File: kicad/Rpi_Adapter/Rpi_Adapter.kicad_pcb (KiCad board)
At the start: 2 copper layers, 42 x 68 mm, 8 parts, among them P1 CONN_02X20, P2 CONN_02X03

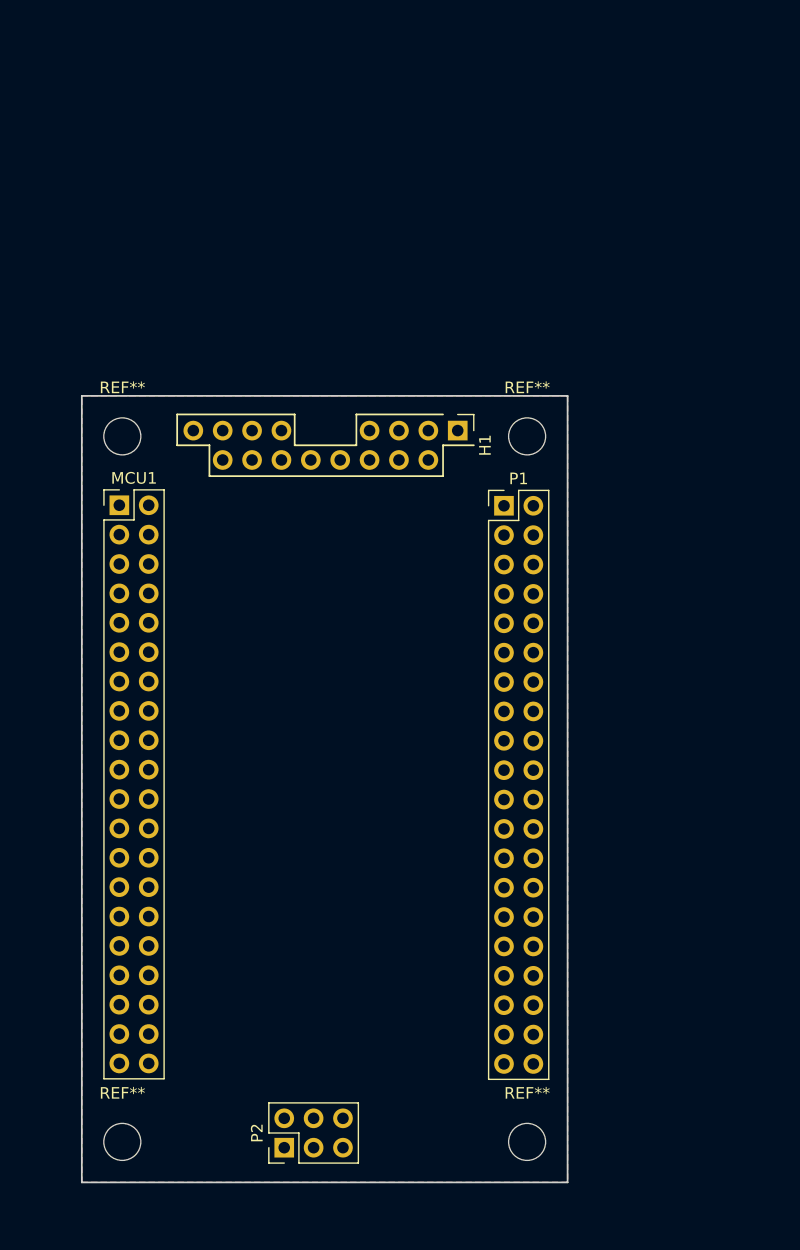
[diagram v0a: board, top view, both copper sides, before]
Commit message: Layout done and 2L_1 is sent to OSH Park
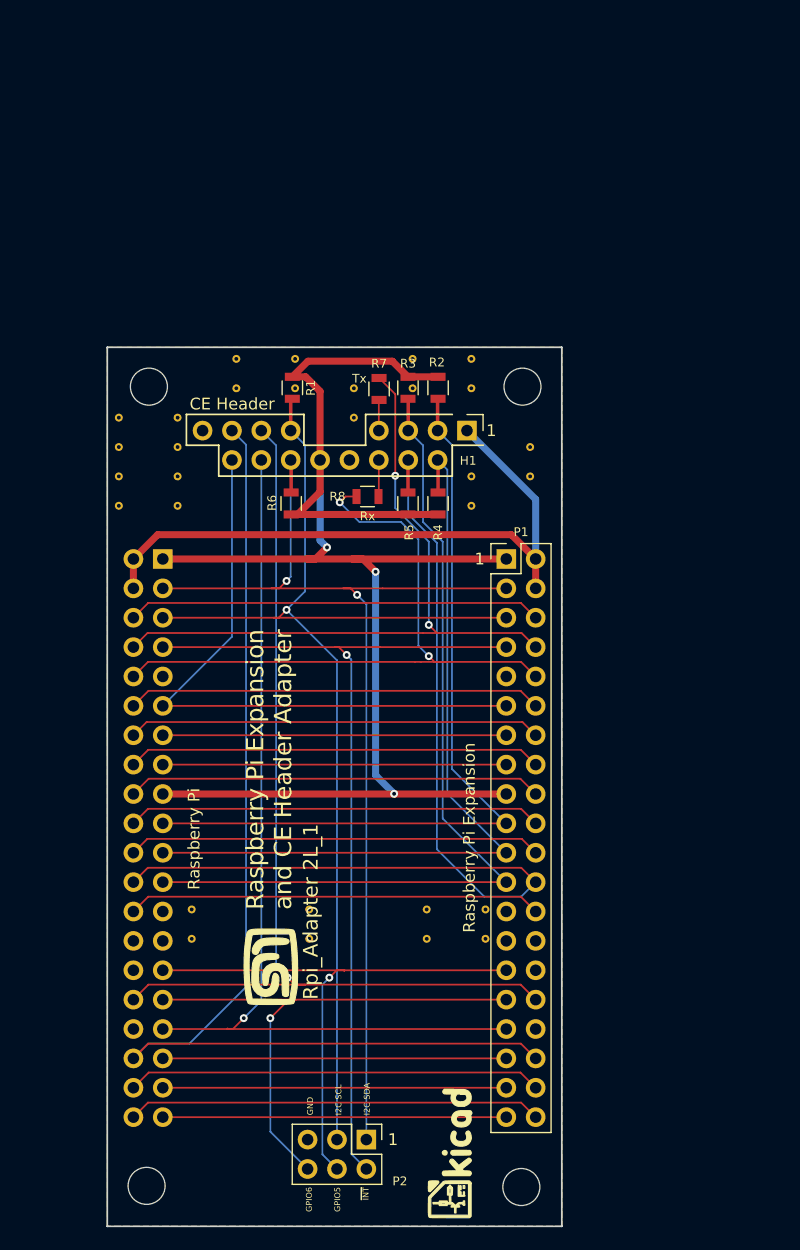
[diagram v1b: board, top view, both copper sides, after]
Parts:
- added 1: Stitch, Rpi_Adapter_Footprints:Stitch, F.Cu at (170.5, 97.4)
- added 11: Stitch, Rpi_Adapter_Footprints:Stitch, F.Cu at (190.8, 99.9)
- added 12: Stitch, Rpi_Adapter_Footprints:Stitch, F.Cu at (195.9, 99.9)
- added 3: Stitch, Rpi_Adapter_Footprints:Stitch, F.Cu at (180.7, 97.4)
- added 5: Stitch, Rpi_Adapter_Footprints:Stitch, F.Cu at (190.8, 97.4)
- added 6: Stitch, Rpi_Adapter_Footprints:Stitch, F.Cu at (195.9, 97.4)
- added 7: Stitch, Rpi_Adapter_Footprints:Stitch, F.Cu at (170.5, 99.9)
- added 9: Stitch, Rpi_Adapter_Footprints:Stitch, F.Cu at (180.7, 99.9)
- added ?: Stitch, Rpi_Adapter_Footprints:Stitch, F.Cu at (194.7, 62.5)
- added ?: Stitch, Rpi_Adapter_Footprints:Stitch, F.Cu at (164.2, 57.4)
- added ?: Stitch, Rpi_Adapter_Footprints:Stitch, F.Cu at (184.5, 54.9)
- added ?: Stitch, Rpi_Adapter_Footprints:Stitch, F.Cu at (169.3, 54.9)
- added ?: Stitch, Rpi_Adapter_Footprints:Stitch, F.Cu at (164.2, 54.9)
- added ?: Stitch, Rpi_Adapter_Footprints:Stitch, F.Cu at (194.7, 52.3)
- added ?: Stitch, Rpi_Adapter_Footprints:Stitch, F.Cu at (189.6, 52.3)
- added ?: Stitch, Rpi_Adapter_Footprints:Stitch, F.Cu at (184.5, 52.3)
- added ?: Stitch, Rpi_Adapter_Footprints:Stitch, F.Cu at (179.4, 52.3)
- added ?: Stitch, Rpi_Adapter_Footprints:Stitch, F.Cu at (174.4, 52.3)
- added ?: Stitch, Rpi_Adapter_Footprints:Stitch, F.Cu at (194.7, 49.8)
- added ?: Stitch, Rpi_Adapter_Footprints:Stitch, F.Cu at (169.3, 62.5)
- added ?: Stitch, Rpi_Adapter_Footprints:Stitch, F.Cu at (189.6, 49.8)
- added ?: Stitch, Rpi_Adapter_Footprints:Stitch, F.Cu at (179.4, 49.8)
- added ?: Stitch, Rpi_Adapter_Footprints:Stitch, F.Cu at (174.4, 49.8)
- added ?: LOGO, Rpi_Adapter_Footprints:KiCad-Logo, F.Cu at (192.8, 118.5)
- added ?: Stitch, Rpi_Adapter_Footprints:Stitch, F.Cu at (164.2, 62.5)
- added ?: Stitch, Rpi_Adapter_Footprints:Stitch, F.Cu at (199.8, 60.0)
- added ?: Stitch, Rpi_Adapter_Footprints:Stitch, F.Cu at (194.7, 60.0)
- added ?: Stitch, Rpi_Adapter_Footprints:Stitch, F.Cu at (169.3, 60.0)
- added ?: Stitch, Rpi_Adapter_Footprints:Stitch, F.Cu at (164.2, 60.0)
- added ?: Stitch, Rpi_Adapter_Footprints:Stitch, F.Cu at (199.8, 57.4)
- added ?: Stitch, Rpi_Adapter_Footprints:Stitch, F.Cu at (169.3, 57.4)
- added G***: LOGO, Rpi_Adapter_Footprints:MyBasic_rounded_50_1, F.Cu at (177.3, 102.4)
- added R1: 4k7, Resistors_SMD:R_0805, F.Cu at (179.2, 52.3)
- added R2: 4k7, Resistors_SMD:R_0805, F.Cu at (191.8, 52.3)
- added R3: 4k7, Resistors_SMD:R_0805, F.Cu at (189.2, 52.3)
- added R4: 4k7, Resistors_SMD:R_0805, F.Cu at (191.8, 62.3)
- added R5: 4k7, Resistors_SMD:R_0805, F.Cu at (189.2, 62.3)
- added R6: 4k7, Resistors_SMD:R_0805, F.Cu at (179.1, 62.3)
- added R7: 0, Resistors_SMD:R_0805, F.Cu at (186.7, 52.4)
- added R8: 0, Resistors_SMD:R_0805, F.Cu at (185.7, 61.7)
- MCU1: moved to B.Cu
- moved P2 7.13 mm to (185.6, 117.3), turned to 270 degrees
- moved MCU1 5.97 mm to (168.0, 67.1), turned to 180 degrees
- moved ? 4.88 mm to (166.8, 52.2)
- moved P1 4.60 mm to (197.7, 67.1)
- moved ? 4.34 mm to (166.6, 121.3)
- moved ? 4.32 mm to (199.1, 52.2)
- moved ? 3.93 mm to (199.0, 121.4)
- moved H1 0.80 mm to (194.3, 56.0)
- renumbered REF** to ?
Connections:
- H1 pad 7: /UART0_Tx -> Net-(H1-Pad7)
- H1 pad 8: /UART0_Rx -> Net-(H1-Pad8)
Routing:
- net GND: track 0.00 -> 137.1 mm
- net /3V3: track 0.00 -> 133.0 mm, vias 0 -> 3
- net /I2C1_SCL: track 0.00 -> 98.2 mm, vias 0 -> 1
- net /GPIO_16: track 0.00 -> 96.7 mm
- net /I2C1_SDA: track 0.00 -> 93.5 mm, vias 0 -> 2
- net /GPIO_12: track 0.00 -> 85.8 mm, vias 0 -> 1
- net /SPI0_CS0: track 0.00 -> 84.1 mm
- net /GPIO_13: track 0.00 -> 80.4 mm, vias 0 -> 1
- net /GPIO_4: track 0.00 -> 76.2 mm, vias 0 -> 1
- net /SPI0_SCLK: track 0.00 -> 75.0 mm
- net /SPI0_MISO: track 0.00 -> 68.9 mm
- net /SPI0_MOSI: track 0.00 -> 68.9 mm
- net /UART0_Tx: track 0.00 -> 60.1 mm, vias 0 -> 2
- net /UART0_Rx: track 0.00 -> 57.7 mm, vias 0 -> 2
- net /5V: track 0.00 -> 55.2 mm
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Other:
- board size 42 x 68 mm -> 39.3 x 76 mm
- rule pad_to_mask_clearance: 0.2 -> 0
- board text added: "1"
- board text added: "CE Header"
- board text added: "GND I2C SCL I2C SDA"
- board text added: "GPIO6 GPIO5 ~INT"
- board text added: "Raspberry Pi"
- board text added: "Raspberry Pi Expansion"
- board text added: "Raspberry Pi Expansion and CE Header Adapter"
- board text added: "Rpi_Adapter 2L_1"
- board text added: "Rx"
- board text added: "Tx"

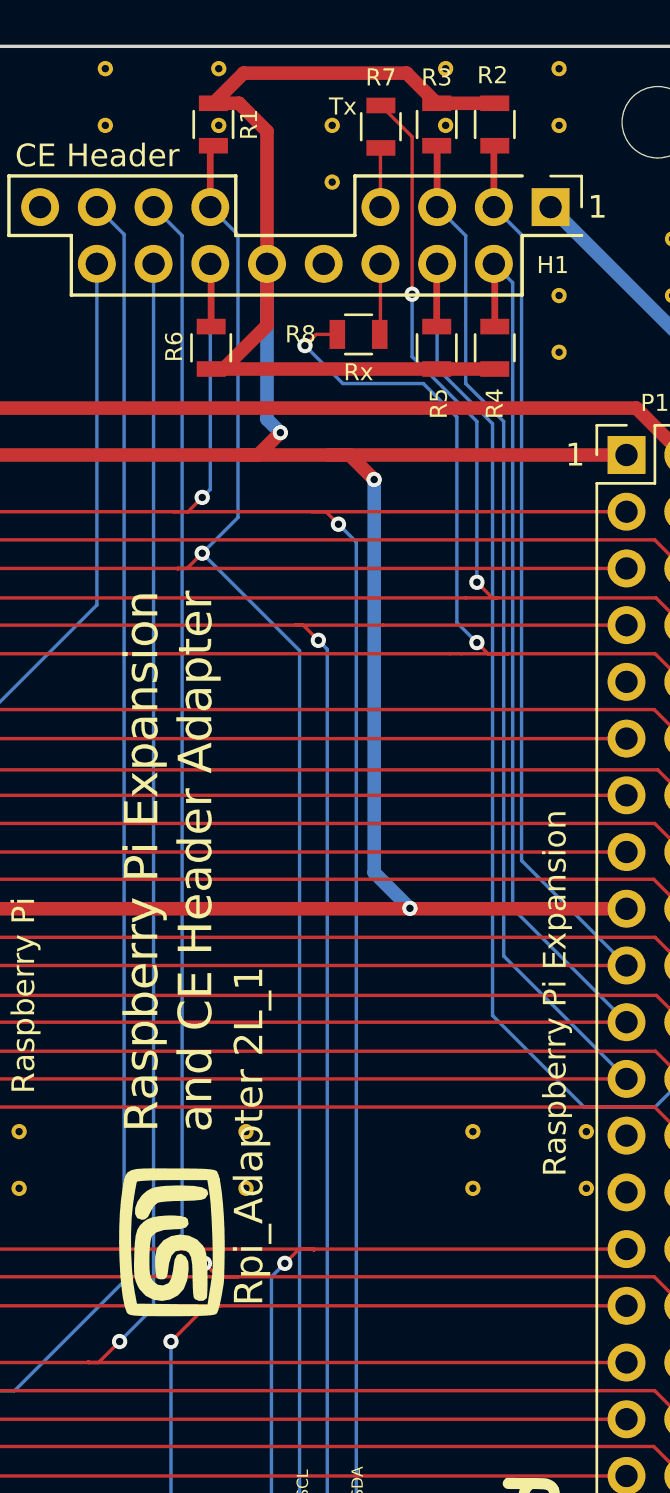
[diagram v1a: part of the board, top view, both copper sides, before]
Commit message: Set the Rx and Tx resistors together incase of swapping
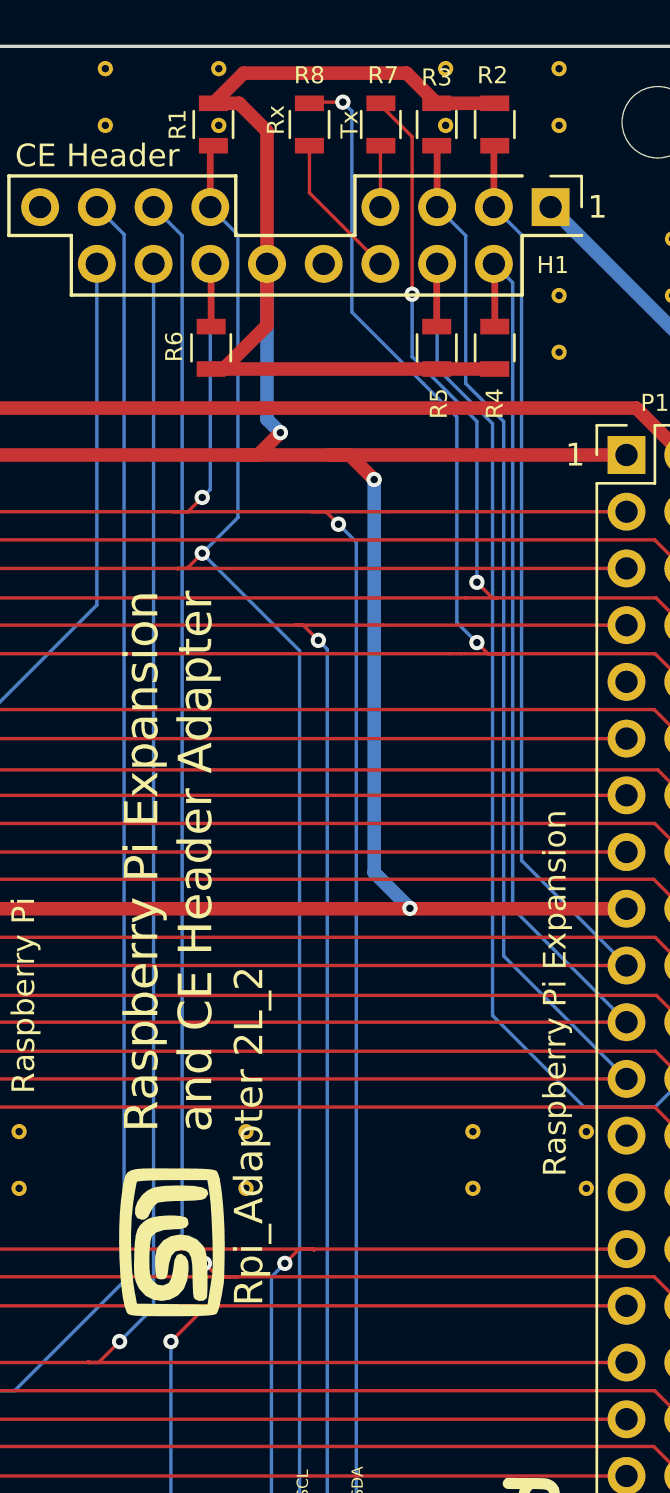
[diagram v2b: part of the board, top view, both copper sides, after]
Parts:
- removed the ? at (184.5, 54.9)
- removed the ? at (184.5, 52.3)
- moved R8 9.65 mm to (183.5, 52.3), turned to 270 degrees
- moved R7 0.10 mm to (186.7, 52.3)
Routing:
- net /UART0_Rx: track 57.7 -> 65.6 mm
- net Net-(H1-Pad8): track 3.17 -> 6.61 mm
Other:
- board text added: "Rpi_Adapter 2L_2"
- board text removed: "Rpi_Adapter 2L_1"
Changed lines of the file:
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@@
 (kicad_pcb (version 4) (host pcbnew 4.0.0-rc1-stable)
   (general
-    (links 113)
+    (links 111)
     (no_connects 0)
-    (area 163.124999 48.724999 202.575001 124.875001)
+    (area 159.253957 47.4237 206.446044 126.3493)
     (thickness 1.6)
     (drawings 17)
-    (tracks 227)
+    (tracks 228)
     (zones 0)
-    (modules 48)
+    (modules 46)
     (nets 36)
   )
@@
   )
   (module Rpi_Adapter_Footprints:Stitch (layer F.Cu)
-    (at 184.52 54.88)
-    (fp_text reference "" (at 0 1.5) (layer Eco1.User) hide
-      (effects (font (size 0.762 0.762) (thickness 0.127)))
-    )
-    (fp_text value Stitch (at 0 -1.5) (layer Eco1.User) hide
-      (effects (font (size 0.762 0.762) (thickness 0.127)))
-    )
-    (pad 1 thru_hole circle (at 0 0) (size 0.6858 0.6858) (drill 0.3302) (layers *.Cu F.SilkS)
-      (net 8 GND) (zone_connect 2))
-  )
-  (module Rpi_Adapter_Footprints:Stitch (layer F.Cu)
     (at 169.28 54.88)
     (fp_text reference "" (at 0 1.5) (layer Eco1.User) hide
@@
   (module Rpi_Adapter_Footprints:Stitch (layer F.Cu)
     (at 189.6 52.34)
-    (fp_text reference "" (at 0 1.5) (layer Eco1.User) hide
-      (effects (font (size 0.762 0.762) (thickness 0.127)))
-    )
-    (fp_text value Stitch (at 0 -1.5) (layer Eco1.User) hide
-      (effects (font (size 0.762 0.762) (thickness 0.127)))
-    )
-    (pad 1 thru_hole circle (at 0 0) (size 0.6858 0.6858) (drill 0.3302) (layers *.Cu F.SilkS)
-      (net 8 GND) (zone_connect 2))
-  )
-  (module Rpi_Adapter_Footprints:Stitch (layer F.Cu)
-    (at 184.52 52.34)
     (fp_text reference "" (at 0 1.5) (layer Eco1.User) hide
       (effects (font (size 0.762 0.762) (thickness 0.127)))
@@
     (tags "resistor 0805")
     (attr smd)
-    (fp_text reference R1 (at 0 -1.6 270) (layer F.SilkS)
+    (fp_text reference R1 (at 0 1.6 270) (layer F.SilkS)
       (effects (font (size 0.762 0.762) (thickness 0.127)))
     )
@@
   )
   (module Resistors_SMD:R_0805 (layer F.Cu)
-    (at 186.7 52.4 90)
+    (at 186.7 52.3 90)
     (descr "Resistor SMD 0805, reflow soldering, Vishay (see dcrcw.pdf)")
     (tags "resistor 0805")
     (attr smd)
-    (fp_text reference R7 (at 2.2 0 180) (layer F.SilkS)
+    (fp_text reference R7 (at 2.2 0.1 360) (layer F.SilkS)
       (effects (font (size 0.762 0.762) (thickness 0.127)))
     )
@@
   )
   (module Resistors_SMD:R_0805 (layer F.Cu)
-    (at 185.7 61.7)
+    (at 183.5 52.3 270)
     (descr "Resistor SMD 0805, reflow soldering, Vishay (see dcrcw.pdf)")
     (tags "resistor 0805")
     (attr smd)
-    (fp_text reference R8 (at -2.6 0) (layer F.SilkS)
-      (effects (font (size 0.762 0.762) (thickness 0.127)))
-    )
-    (fp_text value 0 (at 0 1.75) (layer F.Fab)
-      (effects (font (size 0.762 0.762) (thickness 0.127)))
-    )
-    (fp_text user %R (at 0 0) (layer F.Fab)
+    (fp_text reference R8 (at -2.2 0 360) (layer F.SilkS)
+      (effects (font (size 0.762 0.762) (thickness 0.127)))
+    )
+    (fp_text value 0 (at 0 1.75 270) (layer F.Fab)
+      (effects (font (size 0.762 0.762) (thickness 0.127)))
+    )
+    (fp_text user %R (at 0 0 270) (layer F.Fab)
       (effects (font (size 0.762 0.762) (thickness 0.127)))
     )
@@
     (fp_line (start 1.55 0.9) (end 1.55 -0.9) (layer F.CrtYd) (width 0.05))
     (fp_line (start 1.55 0.9) (end -1.55 0.9) (layer F.CrtYd) (width 0.05))
-    (pad 1 smd rect (at -0.95 0) (size 0.7 1.3) (layers F.Cu F.Paste F.Mask)
+    (pad 1 smd rect (at -0.95 0 270) (size 0.7 1.3) (layers F.Cu F.Paste F.Mask)
       (net 7 /UART0_Rx))
-    (pad 2 smd rect (at 0.95 0) (size 0.7 1.3) (layers F.Cu F.Paste F.Mask)
+    (pad 2 smd rect (at 0.95 0 270) (size 0.7 1.3) (layers F.Cu F.Paste F.Mask)
       (net 35 "Net-(H1-Pad8)"))
     (model ${KISYS3DMOD}/Resistors_SMD.3dshapes/R_0805.wrl
@@
     )
   )
-  (gr_text Tx (at 185 51.5) (layer F.SilkS)
+  (gr_text Tx (at 185.3 52.3 90) (layer F.SilkS)
     (effects (font (size 0.762 0.762) (thickness 0.127)))
   )
-  (gr_text Rx (at 185.7 63.4) (layer F.SilkS)
+  (gr_text Rx (at 182 52.1 90) (layer F.SilkS)
     (effects (font (size 0.762 0.762) (thickness 0.127)))
   )
-  (gr_text "Rpi_Adapter 2L_1" (at 180.8 97.6 90) (layer F.SilkS)
+  (gr_text "Rpi_Adapter 2L_2" (at 180.8 97.6 90) (layer F.SilkS)
     (effects (font (size 1.27 1.27) (thickness 0.127)))
   )
@@
   (segment (start 190.5 73.5) (end 191.9 73.5) (width 0.1524) (layer F.Cu) (net 6))
   (segment (start 191.9 73.5) (end 199.02 73.5) (width 0.1524) (layer F.Cu) (net 6))
-  (segment (start 184.75 61.7) (end 183.8 61.7) (width 0.1524) (layer F.Cu) (net 7))
-  (segment (start 191.5 76) (end 192.4 76) (width 0.1524) (layer F.Cu) (net 7))
+  (segment (start 188.6 63.9) (end 185.4 60.7) (width 0.1524) (layer B.Cu) (net 7))
+  (segment (start 192.4 76) (end 191.5 76) (width 0.1524) (layer F.Cu) (net 7))
   (segment (start 191 75.5) (end 191.5 76) (width 0.1524) (layer F.Cu) (net 7))
   (via (at 191 75.5) (size 0.6858) (drill 0.3302) (layers F.Cu B.Cu) (net 7))
@@
   (segment (start 190.1 65.4) (end 190.1 74.6) (width 0.1524) (layer B.Cu) (net 7))
   (segment (start 188.6 63.9) (end 190.1 65.4) (width 0.1524) (layer B.Cu) (net 7))
-  (segment (start 185 63.9) (end 188.6 63.9) (width 0.1524) (layer B.Cu) (net 7))
-  (segment (start 183.3 62.2) (end 185 63.9) (width 0.1524) (layer B.Cu) (net 7))
-  (via (at 183.3 62.2) (size 0.6858) (drill 0.3302) (layers F.Cu B.Cu) (net 7))
-  (segment (start 183.8 61.7) (end 183.3 62.2) (width 0.1524) (layer F.Cu) (net 7))
+  (segment (start 185 51.3) (end 183.55 51.3) (width 0.1524) (layer F.Cu) (net 7))
+  (via (at 185 51.3) (size 0.6858) (drill 0.3302) (layers F.Cu B.Cu) (net 7))
+  (segment (start 185.4 51.7) (end 185 51.3) (width 0.1524) (layer B.Cu) (net 7))
+  (segment (start 185.4 60.7) (end 185.4 51.7) (width 0.1524) (layer B.Cu) (net 7))
+  (segment (start 183.55 51.3) (end 183.5 51.35) (width 0.1524) (layer F.Cu) (net 7))
   (segment (start 165.46 77.26) (end 166.72 76) (width 0.1524) (layer F.Cu) (net 7))
   (segment (start 198.98 76) (end 200.24 77.26) (width 0.1524) (layer F.Cu) (net 7))
@@
   (segment (start 186.7 53.35) (end 186.68 53.37) (width 0.1524) (layer F.Cu) (net 34))
   (segment (start 186.68 53.37) (end 186.68 56) (width 0.1524) (layer F.Cu) (net 34))
-  (segment (start 186.68 58.54) (end 186.68 61.67) (width 0.1524) (layer F.Cu) (net 35))
-  (segment (start 186.68 61.67) (end 186.65 61.7) (width 0.1524) (layer F.Cu) (net 35))
+  (segment (start 183.5 53.25) (end 183.5 55.36) (width 0.1524) (layer F.Cu) (net 35))
+  (segment (start 183.5 55.36) (end 186.68 58.54) (width 0.1524) (layer F.Cu) (net 35))
   (zone (net 8) (net_name GND) (layer B.Cu) (hatch edge 0.508)
     (connect_pads (clearance 0.254))
